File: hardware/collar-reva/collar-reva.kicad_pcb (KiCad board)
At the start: 2 copper layers, 30 x 30 mm, 0 parts

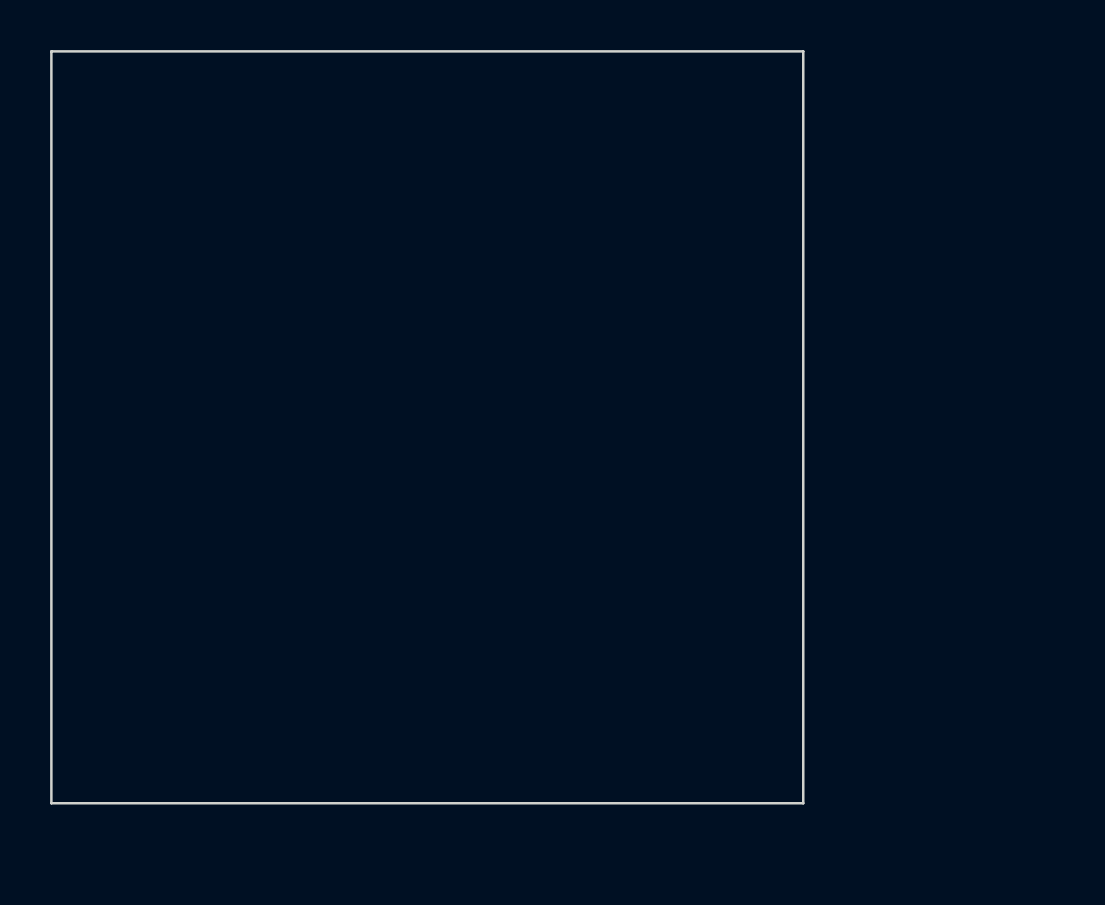
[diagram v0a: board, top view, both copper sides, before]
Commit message: feat(collar): ESP32-S3 firmware and neck PPG (#34)
* feat(collar): ESP32-S3 firmware and TI AFE4404 neck PPG

Host-tested HR/HRV, IMU RMS, and 1 Hz frames plus Arduino bring-up. Schematic adds the ventral-neck optical AFE on I2C so the puck can read pulse without actuation.

Co-authored-by: Cursor <cursoragent@cursor.com>

* feat(firmware): wire IMU, VBAT, and audio features into the collar loop

Bring-up now reads BMI270 accel and AFE4404 IR, converts VBAT on the derived divider, and keeps BLE notify-only.

Co-authored-by: Cursor <cursoragent@cursor.com>

* feat(firmware): I2S mic hop and VBAT-empty fault priority

INMP441 now feeds audio RMS/bark on the Rev-A pin map, and a low cell overrides a missing PPG peak so the 1 Hz frame reports the more urgent fault.

Co-authored-by: Cursor <cursoragent@cursor.com>

* feat(firmware): emit Phase-2 CBOR frames and check BMI270 chip ID

The 1 Hz notify is a real CBOR map (not JSON), and bring-up NAKs a missing IMU so we do not silently stream zeros.

Co-authored-by: Cursor <cursoragent@cursor.com>

* docs(firmware): note I2S RX pins in the collar bring-up order

Co-authored-by: Cursor <cursoragent@cursor.com>

* feat(firmware): pack 1 Hz CBOR to a BLE notify MTU

Frames now clip to MTU-3 so a default 23-byte ATT MTU cannot silently truncate the Phase-2 map once NimBLE is attached.

Co-authored-by: Cursor <cursoragent@cursor.com>

* feat(firmware): NimBLE advertise aarf-collar and notify 1 Hz CBOR

Phone can subscribe to the notify-only GATT char. LED and WDT follow the fault table, and IMU/mic NAKs now beat a missing PPG peak.

Co-authored-by: Cursor <cursoragent@cursor.com>

* feat(firmware): BMI270 accel bring-up and NVS VBAT cal

Soft-reset and enable ±8 g accel after chip-ID, and load divider scale/offset from NVS so bench cal survives reboot. PlatformIO build stays green.

Co-authored-by: Cursor <cursoragent@cursor.com>

* feat(firmware): bark CLIP to /infer/audio plus AFE4404 4 mA init

Wi-Fi posts the existing runtime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
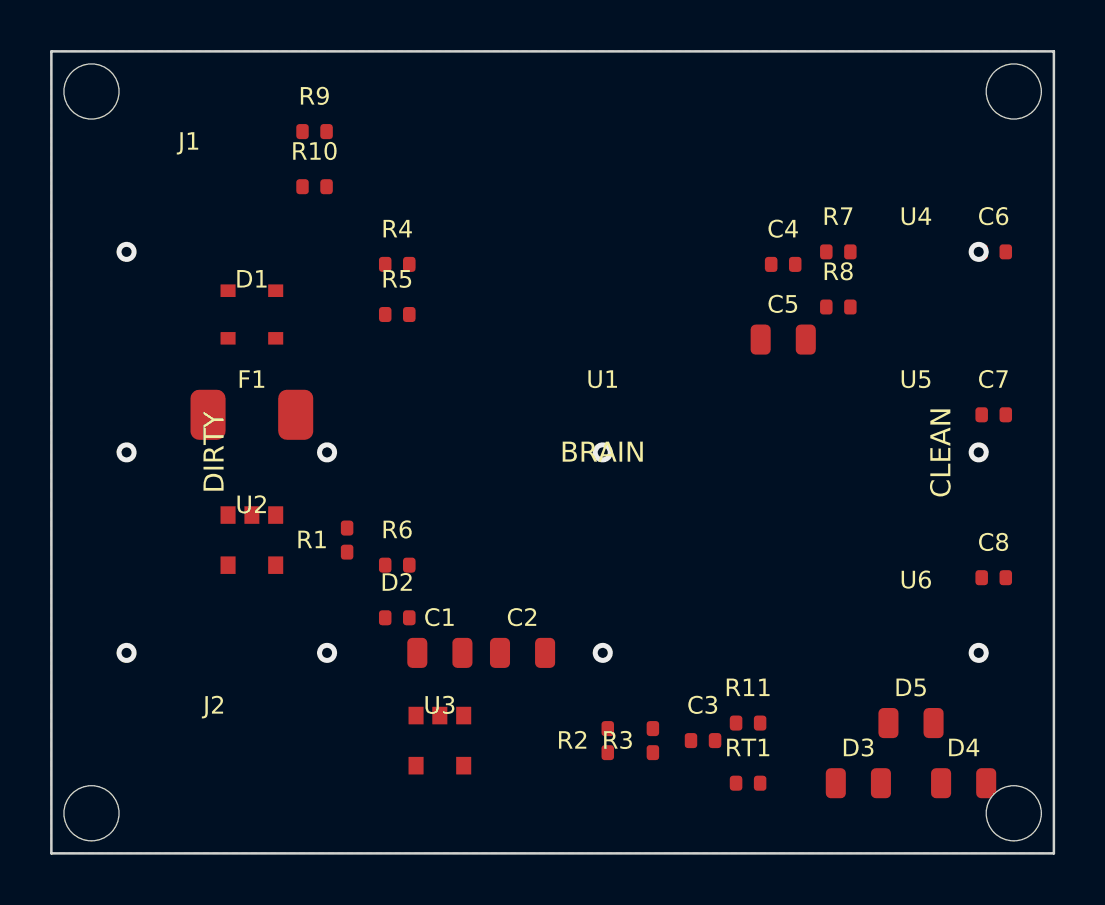
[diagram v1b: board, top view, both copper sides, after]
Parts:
- added C1: 10uF 16V, Capacitor_SMD:C_0805_2012Metric, F.Cu at (115.5, 104.0)
- added C2: 10uF 16V, Capacitor_SMD:C_0805_2012Metric, F.Cu at (118.8, 104.0)
- added C3: 100nF 16V, Capacitor_SMD:C_0402_1005Metric, F.Cu at (126.0, 107.5)
- added C4: 100nF 16V, Capacitor_SMD:C_0402_1005Metric, F.Cu at (129.2, 88.5)
- added C5: 10uF 16V, Capacitor_SMD:C_0805_2012Metric, F.Cu at (129.2, 91.5)
- added C6: 100nF 16V, Capacitor_SMD:C_0402_1005Metric, F.Cu at (137.6, 88.0)
- added C7: 100nF 16V, Capacitor_SMD:C_0402_1005Metric, F.Cu at (137.6, 94.5)
- added C8: 100nF 16V, Capacitor_SMD:C_0402_1005Metric, F.Cu at (137.6, 101.0)
- added D1: USBLC6-2SC6, Package_TO_SOT_SMD:SOT-23-6, F.Cu at (108.0, 90.5)
- added D2: Green LED, LED_SMD:LED_0402_1005Metric, F.Cu at (113.8, 102.6)
- added D3: 940 nm IR LED, LED_SMD:LED_0805_2012Metric, F.Cu at (132.2, 109.2)
- added D4: 940 nm photodiode, Diode_SMD:D_0805_2012Metric, F.Cu at (136.4, 109.2)
- added D5: 660 nm red LED, LED_SMD:LED_0805_2012Metric, F.Cu at (134.3, 106.8)
- added F1: PTC 500 mA, Fuse:Fuse_1812_4532Metric, F.Cu at (108.0, 94.5)
- added H: , MountingHole:MountingHole_2.2mm, F.Cu at (101.6, 81.6)
- added H: , MountingHole:MountingHole_2.2mm, F.Cu at (138.4, 81.6)
- added H: , MountingHole:MountingHole_2.2mm, F.Cu at (101.6, 110.4)
- added H: , MountingHole:MountingHole_2.2mm, F.Cu at (138.4, 110.4)
- added J1: USB-C receptacle, Connector_USB:USB_C_Receptacle_USB4105-xx-A_16P_TopMnt_Horizontal, F.Cu at (105.5, 85.0)
- added J2: JST-PH 2, Connector_JST:JST_PH_S2B-PH-SM4-TB_1x02-1MP_P2.00mm_Horizontal, F.Cu at (106.5, 107.5)
- added R1: 10k, Resistor_SMD:R_0402_1005Metric, F.Cu at (111.8, 99.5)
- added R10: 5.1k, Resistor_SMD:R_0402_1005Metric, F.Cu at (110.5, 85.4)
- added R11: 10k, Resistor_SMD:R_0402_1005Metric, F.Cu at (127.8, 106.8)
- added R2: 100k, Resistor_SMD:R_0402_1005Metric, F.Cu at (122.2, 107.5)
- added R3: 100k, Resistor_SMD:R_0402_1005Metric, F.Cu at (124.0, 107.5)
- added R4: 10k, Resistor_SMD:R_0402_1005Metric, F.Cu at (113.8, 88.5)
- added R5: 10k, Resistor_SMD:R_0402_1005Metric, F.Cu at (113.8, 90.5)
- added R6: 330, Resistor_SMD:R_0402_1005Metric, F.Cu at (113.8, 100.5)
- added R7: 4.7k, Resistor_SMD:R_0402_1005Metric, F.Cu at (131.4, 88.0)
- added R8: 4.7k, Resistor_SMD:R_0402_1005Metric, F.Cu at (131.4, 90.2)
- added R9: 5.1k, Resistor_SMD:R_0402_1005Metric, F.Cu at (110.5, 83.2)
- added RT1: 10k NTC β3950, Resistor_SMD:R_0402_1005Metric, F.Cu at (127.8, 109.2)
- added U1: ESP32-S3-MINI-1-N8, RF_Module:ESP32-S3-MINI-1, F.Cu at (122.0, 94.5)
- added U2: MCP73831 4.2 V, Package_TO_SOT_SMD:SOT-23-5, F.Cu at (108.0, 99.5)
- added U3: AP2112K-3.3 600 mA, Package_TO_SOT_SMD:SOT-23-5, F.Cu at (115.5, 107.5)
- added U4: BMI270, Sensor_Motion:Bosch_LGA-14_2.5x3mm_P0.5mm_ClockwisePinNumbering, F.Cu at (134.5, 88.0)
- added U5: INMP441, Sensor_Audio:InvenSense_INMP441, F.Cu at (134.5, 94.5)
- added U6: AFE4404, Package_BGA:Texas_DSBGA-15_1.91x1.91mm_Layout5x3_P0.4mm, F.Cu at (134.5, 102.5)
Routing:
- net GND: vias 0 -> 10
- added copper zone on B.Cu, net GND
- added copper zone on F.Cu, net GND
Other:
- board size 30 x 30 mm -> 40 x 32 mm
- board text added: "BRAIN"
- board text added: "CLEAN"
- board text added: "DIRTY"
- board text added: "RF_KEEP"
